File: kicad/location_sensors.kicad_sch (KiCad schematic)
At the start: 24 parts

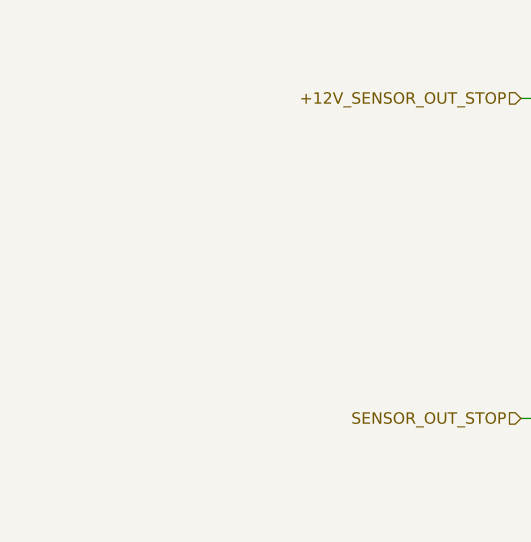
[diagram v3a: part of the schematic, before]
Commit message: Changed power supply chips as the 12V is no longer required.
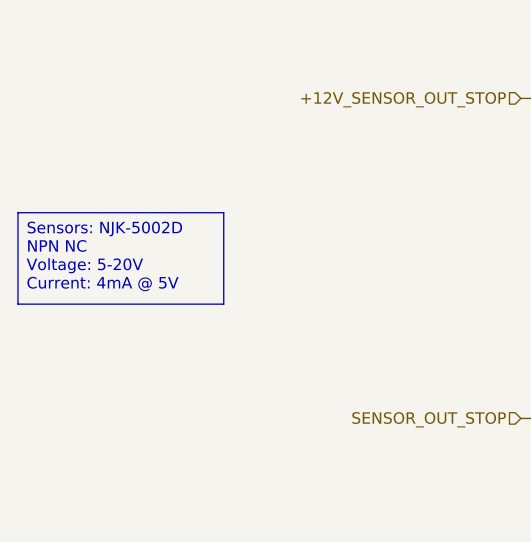
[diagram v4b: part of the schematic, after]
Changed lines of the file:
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@@
 		(company "NX Solutions")
+	)
+	(text_box "Sensors: NJK-5002D NPN NC\nVoltage: 5-20V\nCurrent: 4mA @ 5V"
+		(exclude_from_sim no)
+		(at 21.59 39.37 0)
+		(size 22.86 10.16)
+		(margins 0.9525 0.9525 0.9525 0.9525)
+		(stroke
+			(width 0)
+			(type solid)
+		)
+		(fill
+			(type none)
+		)
+		(effects
+			(font
+				(size 1.27 1.27)
+			)
+			(justify left top)
+		)
 	)
 	(junction

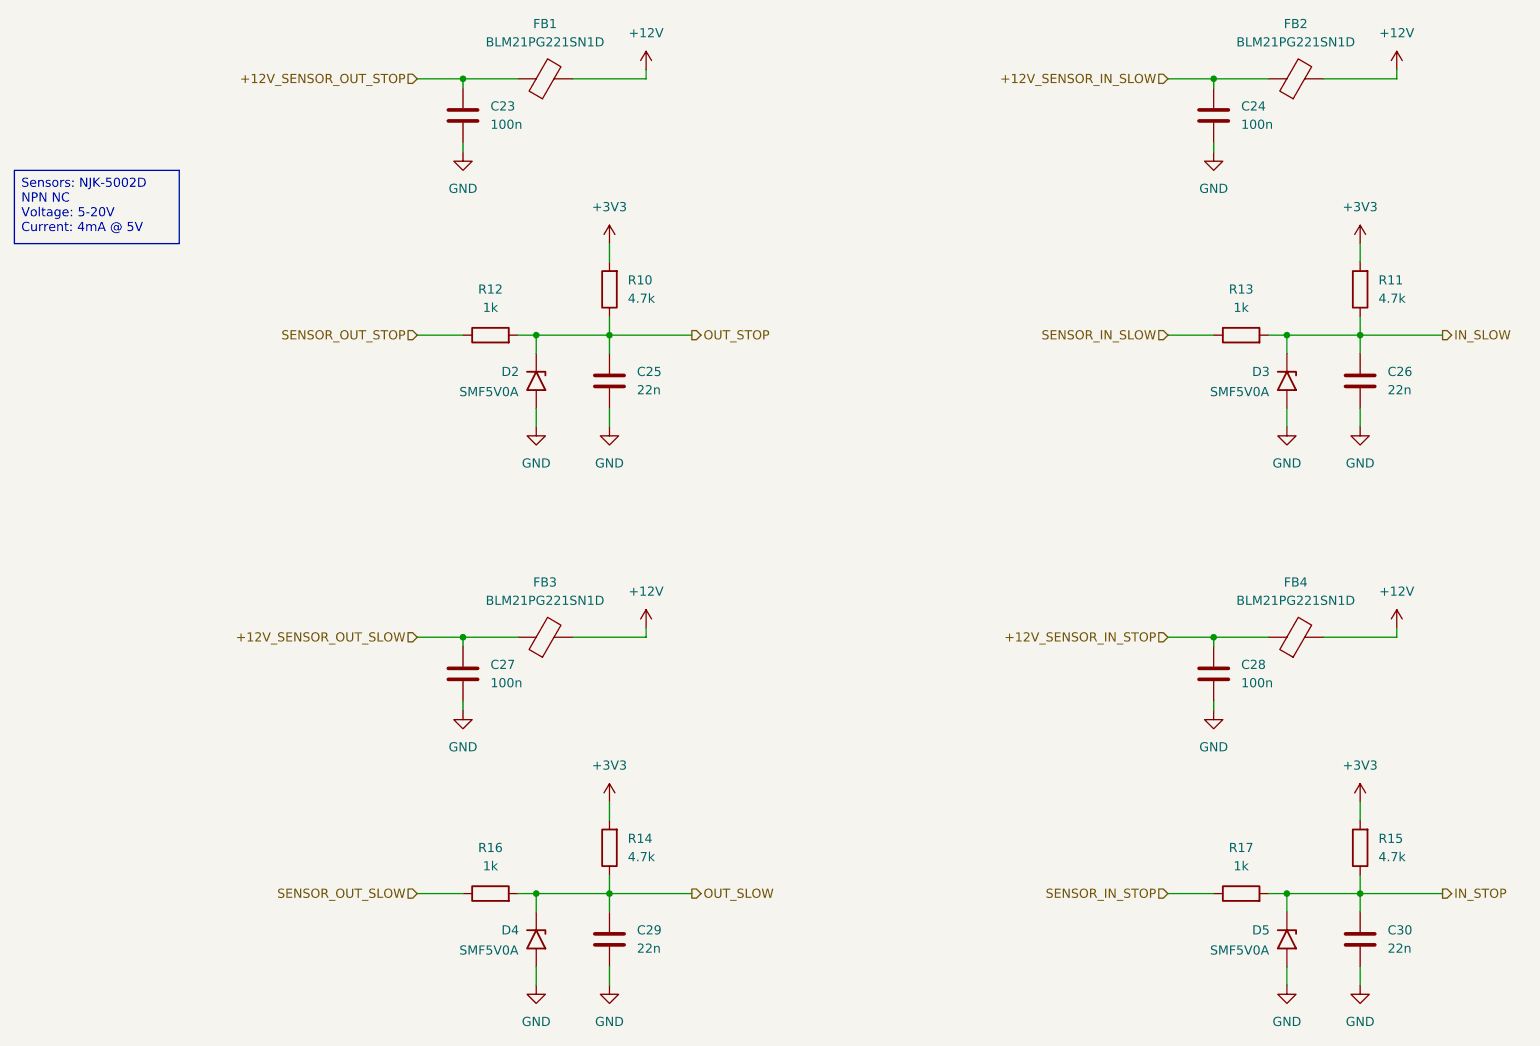
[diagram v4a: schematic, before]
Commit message: Finished the schematic and started the PCB.
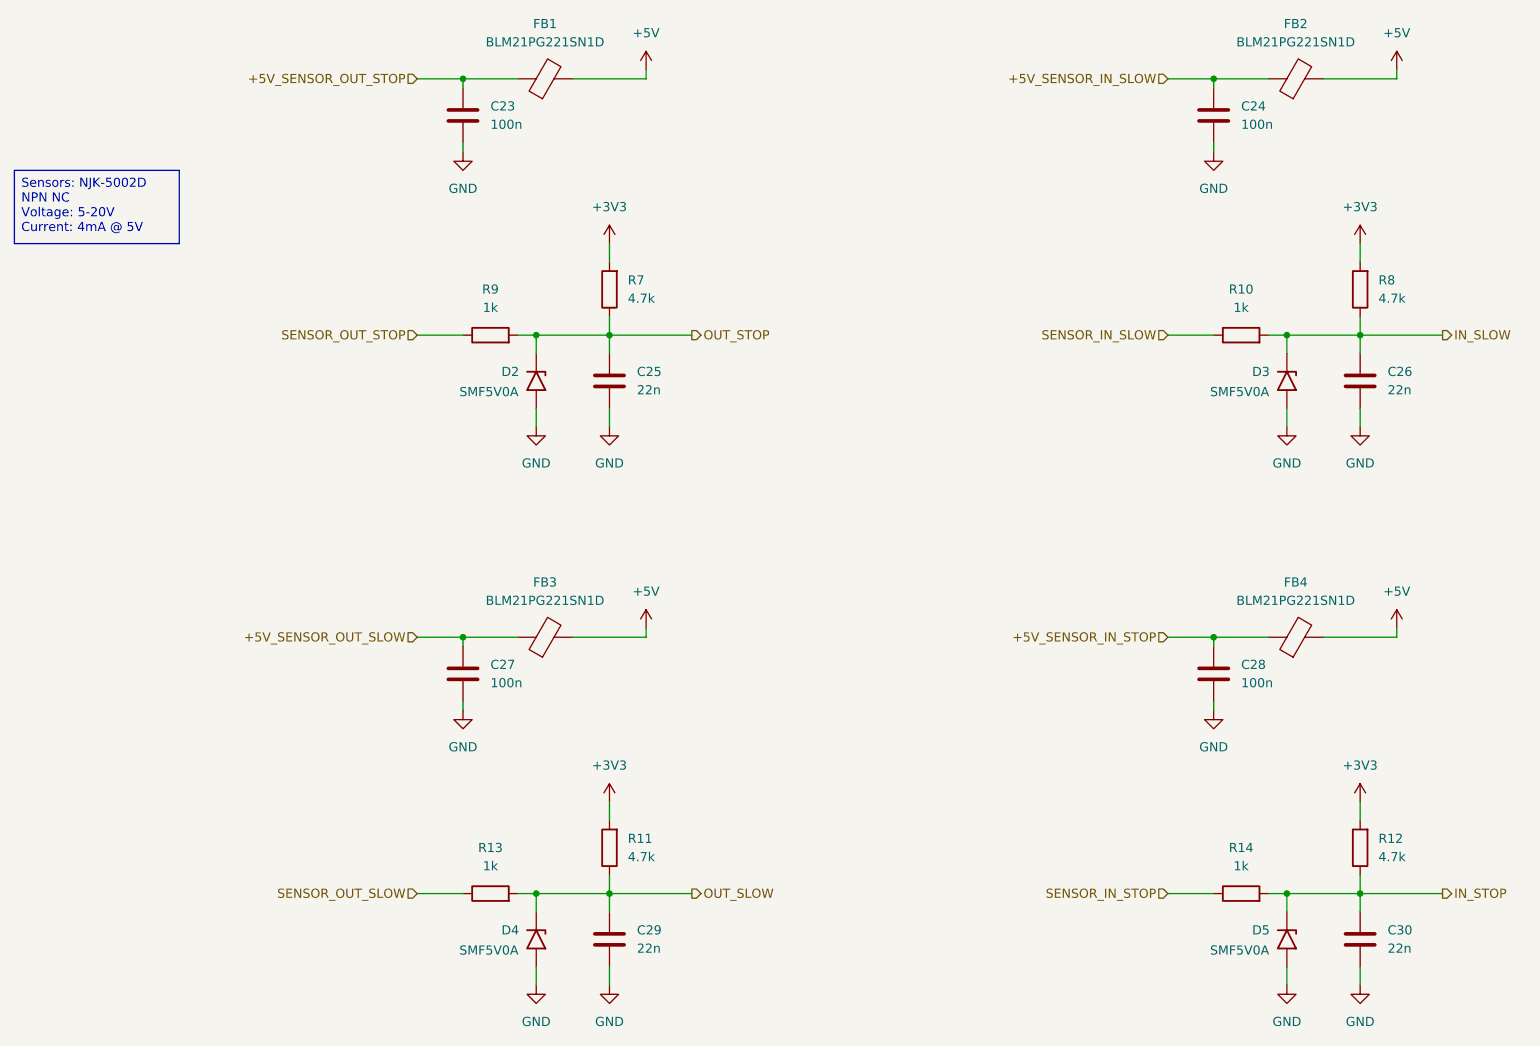
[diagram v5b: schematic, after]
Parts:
- renumbered R13 to R10, R14 to R11, R15 to R12, R16 to R13, R17 to R14, R10 to R7, R11 to R8, R12 to R9
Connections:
- net +12V renamed +5V
- net +12V_SENSOR_IN_SLOW renamed +5V_SENSOR_IN_SLOW
- net +12V_SENSOR_IN_STOP renamed +5V_SENSOR_IN_STOP
- net +12V_SENSOR_OUT_SLOW renamed +5V_SENSOR_OUT_SLOW
- net +12V_SENSOR_OUT_STOP renamed +5V_SENSOR_OUT_STOP

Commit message: Reviewed the part numbers, footprints and pin numbers.
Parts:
- D2, D3, D4, D5: MF (none) -> Vishay; MP (none) -> SMF5V0A-E3-08; Supplier (none) -> Digi-Key; SupplierPN (none) -> SMF5V0A-E3-08CT-ND; Voltage (none) -> 9.2V

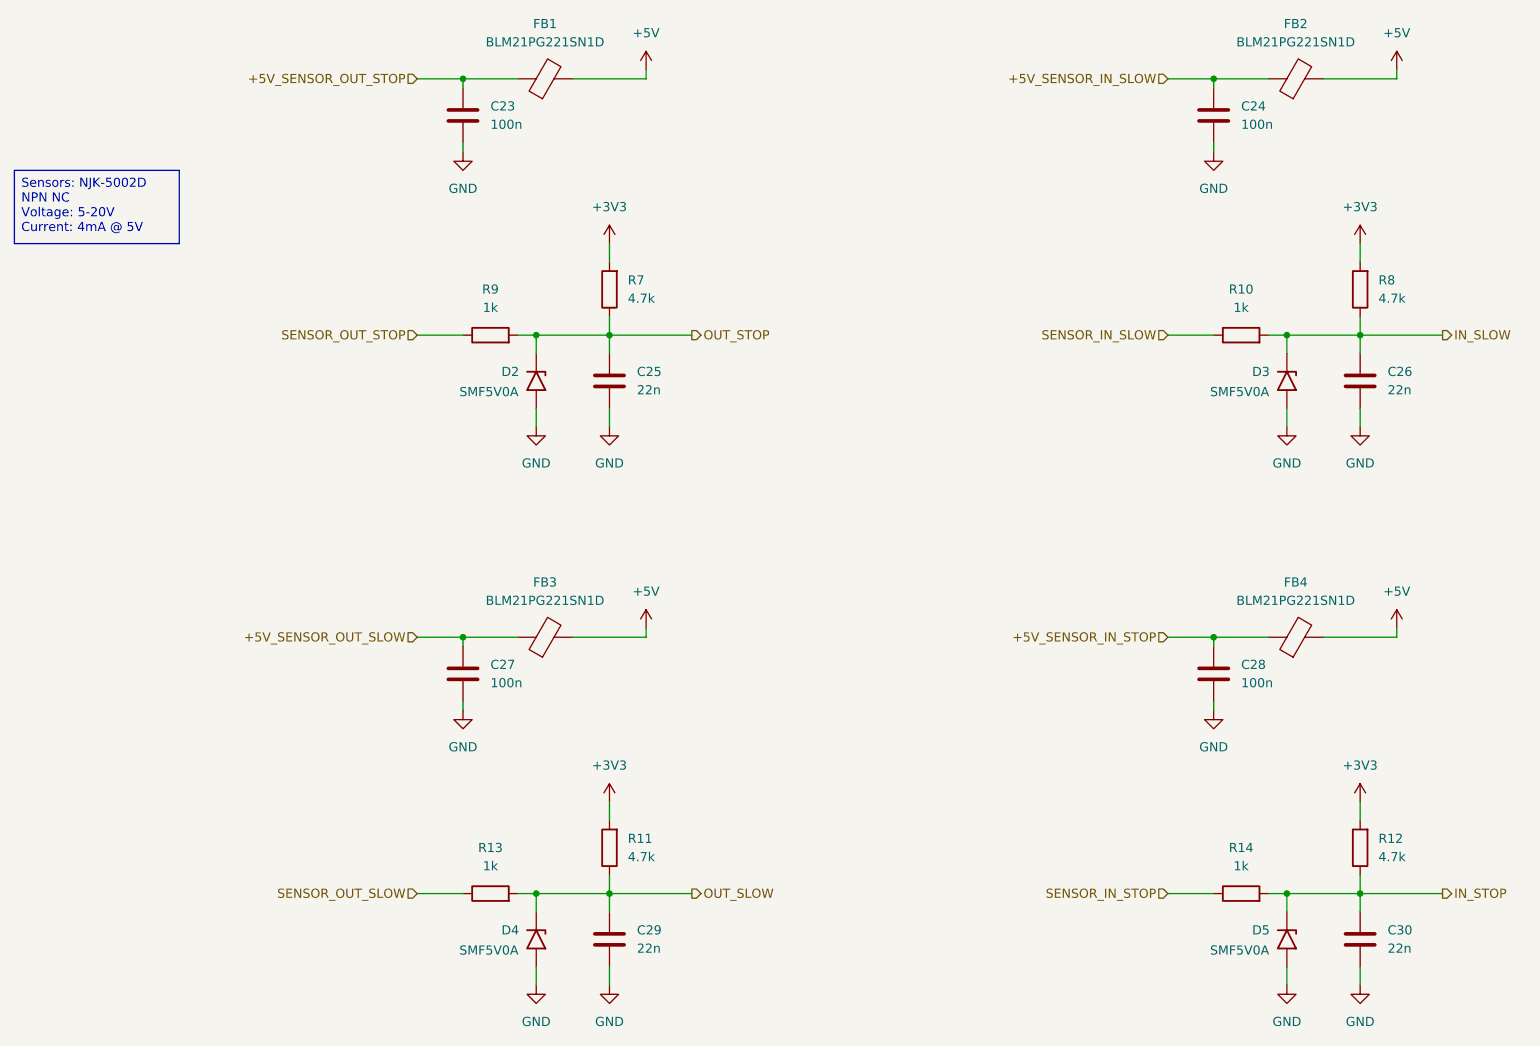
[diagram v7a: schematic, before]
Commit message: Re-annotated and added extra capacitors for the 5V and 3V3 DC-DC converters. Added testpoints to the electronic fuse.
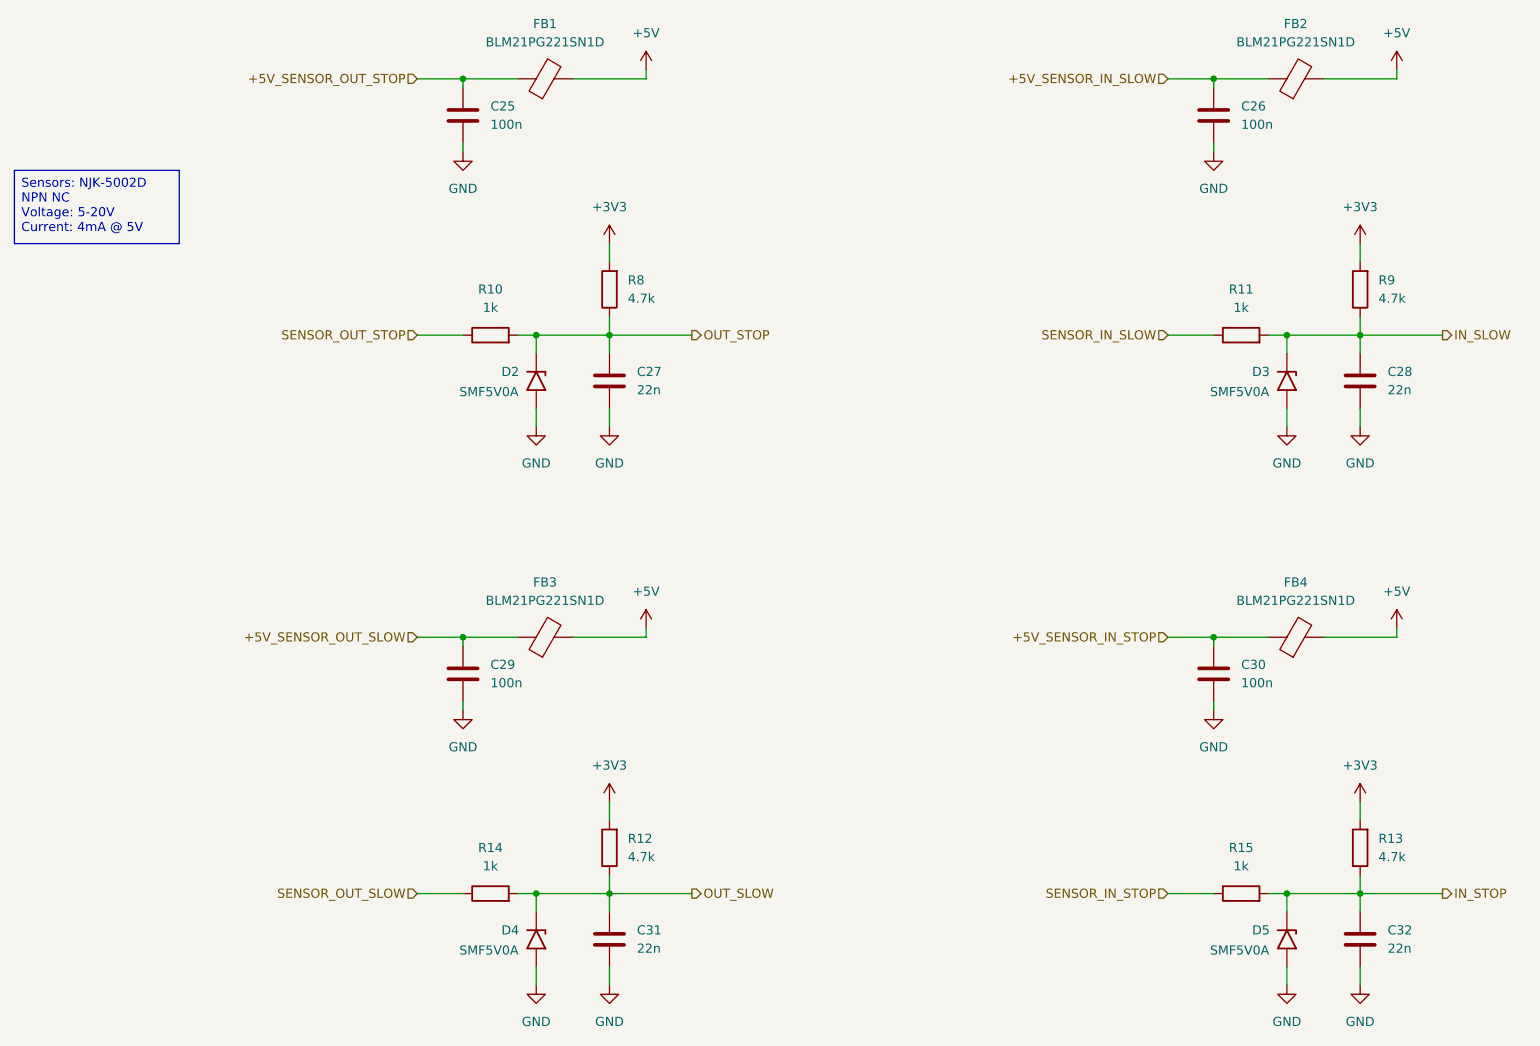
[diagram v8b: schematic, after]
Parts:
- renumbered C23 to C25, C24 to C26, C25 to C27, C26 to C28, C27 to C29, C28 to C30, C29 to C31, C30 to C32, R9 to R10, R10 to R11, R11 to R12, R12 to R13, R13 to R14, R14 to R15, R7 to R8, R8 to R9
